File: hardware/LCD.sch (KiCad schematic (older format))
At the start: 0 parts

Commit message: Se finalizo esquematico del cricuito.
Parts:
- added DS1: LCD16X2, WC1602A, symbol LCD16X2
- added R7: 220, symbol R
- added RV1: 10k, symbol POT
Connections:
- new net: DS1.16 (LED-), R7.1
- new net: DS1.3 (VO), RV1.2
- new net +5V: DS1.15 (LED+), DS1.2 (VDD), RV1.1
- new net D1: DS1.11 (D4)
- new net D2: DS1.12 (D5)
- new net D3: DS1.13 (D6)
- new net D4: DS1.14 (D7)
- new net Ena: DS1.6 (E)
- new net GND: DS1.1 (VSS), DS1.10 (D3), DS1.5 (R/W), DS1.7 (D0), DS1.8 (D1), DS1.9 (D2), R7.2, RV1.3
- new net RS: DS1.4 (RS)
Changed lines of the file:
@@
 $Descr A4 11693 8268
 encoding utf-8
-Sheet 1 5
+Sheet 4 5
 Title ""
-Date ""
+Date "2016-07-04"
 Rev ""
-Comp ""
+Comp "Felipe Rey"
 Comment1 ""
 Comment2 ""
@@
 Comment4 ""
 $EndDescr
+$Comp
+L LCD16X2 DS1
+U 1 1 578E41A0
+P 5400 2050
+F 0 "DS1" H 4600 2450 50  0000 C CNN
+F 1 "LCD16X2" H 6100 2450 50  0000 C CNN
+F 2 "WC1602A" H 5400 2000 50  0000 C CIN
+F 3 "" H 5400 2050 50  0000 C CNN
+	1    5400 2050
+	1    0    0    -1
+$EndComp
+$Comp
+L GND #PWR016
+U 1 1 578E4217
+P 4650 3200
+F 0 "#PWR016" H 4650 2950 50  0001 C CNN
+F 1 "GND" H 4650 3050 50  0000 C CNN
+F 2 "" H 4650 3200 50  0000 C CNN
+F 3 "" H 4650 3200 50  0000 C CNN
+	1    4650 3200
+	1    0    0    -1
+$EndComp
+Wire Wire Line
+	4650 2550 4650 3200
+Wire Wire Line
+	5050 2550 5050 2850
+Wire Wire Line
+	4650 2850 5550 2850
+Connection ~ 4650 2850
+$Comp
+L +5V #PWR017
+U 1 1 578E4237
+P 4200 2150
+F 0 "#PWR017" H 4200 2000 50  0001 C CNN
+F 1 "+5V" H 4200 2290 50  0000 C CNN
+F 2 "" H 4200 2150 50  0000 C CNN
+F 3 "" H 4200 2150 50  0000 C CNN
+	1    4200 2150
+	1    0    0    -1
+$EndComp
+Wire Wire Line
+	4750 2550 4750 2650
+Wire Wire Line
+	4750 2650 4200 2650
+Wire Wire Line
+	4200 2650 4200 2150
+$Comp
+L POT RV1
+U 1 1 578E43FF
+P 3550 2750
+F 0 "RV1" H 3550 2650 50  0000 C CNN
+F 1 "10k" H 3550 2750 50  0000 C CNN
+F 2 "" H 3550 2750 50  0000 C CNN
+F 3 "" H 3550 2750 50  0000 C CNN
+	1    3550 2750
+	0    1    1    0
+$EndComp
+Wire Wire Line
+	4850 2550 4850 2750
+Wire Wire Line
+	4850 2750 3700 2750
+Wire Wire Line
+	3550 3000 3550 3100
+Wire Wire Line
+	3550 3100 4650 3100
+Connection ~ 4650 3100
+Wire Wire Line
+	3550 2500 3550 2250
+Wire Wire Line
+	3550 2250 4200 2250
+Connection ~ 4200 2250
+$Comp
+L +5V #PWR018
+U 1 1 578E496B
+P 6600 2250
+F 0 "#PWR018" H 6600 2100 50  0001 C CNN
+F 1 "+5V" H 6600 2390 50  0000 C CNN
+F 2 "" H 6600 2250 50  0000 C CNN
+F 3 "" H 6600 2250 50  0000 C CNN
+	1    6600 2250
+	1    0    0    -1
+$EndComp
+Wire Wire Line
+	6600 2250 6600 2700
+Wire Wire Line
+	6600 2700 6050 2700
+Wire Wire Line
+	6050 2700 6050 2550
+$Comp
+L R R7
+U 1 1 578E4997
+P 6150 3050
+F 0 "R7" V 6230 3050 50  0000 C CNN
+F 1 "220" V 6150 3050 50  0000 C CNN
+F 2 "" V 6080 3050 50  0000 C CNN
+F 3 "" H 6150 3050 50  0000 C CNN
+	1    6150 3050
+	1    0    0    -1
+$EndComp
+Wire Wire Line
+	6150 2550 6150 2900
+$Comp
+L GND #PWR019
+U 1 1 578E49E7
+P 6150 3400
+F 0 "#PWR019" H 6150 3150 50  0001 C CNN
+F 1 "GND" H 6150 3250 50  0000 C CNN
+F 2 "" H 6150 3400 50  0000 C CNN
+F 3 "" H 6150 3400 50  0000 C CNN
+	1    6150 3400
+	1    0    0    -1
+$EndComp
+Wire Wire Line
+	6150 3400 6150 3200
+Text HLabel 4950 3450 3    60   Input ~ 0
+RS
+Wire Wire Line
+	4950 2550 4950 3450
+Text HLabel 5150 3450 3    60   Input ~ 0
+Ena
+Wire Wire Line
+	5150 2550 5150 3450
+Text HLabel 5650 3500 3    60   Input ~ 0
+D1
+Text HLabel 5750 3500 3    60   Input ~ 0
+D2
+Text HLabel 5850 3500 3    60   Input ~ 0
+D3
+Text HLabel 5950 3500 3    60   Input ~ 0
+D4
+Wire Wire Line
+	5650 2550 5650 3500
+Wire Wire Line
+	5750 2550 5750 3500
+Wire Wire Line
+	5850 2550 5850 3500
+Wire Wire Line
+	5950 2550 5950 3500
+Wire Wire Line
+	5250 2850 5250 2550
+Connection ~ 5050 2850
+Wire Wire Line
+	5350 2850 5350 2550
+Connection ~ 5250 2850
+Wire Wire Line
+	5450 2850 5450 2550
+Connection ~ 5350 2850
+Wire Wire Line
+	5550 2850 5550 2550
+Connection ~ 5450 2850
 $EndSCHEMATC

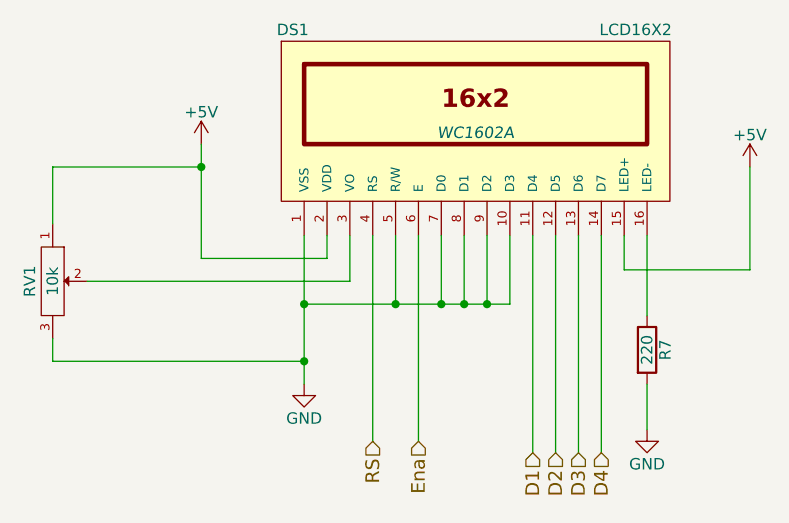
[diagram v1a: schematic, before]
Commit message: Se cargaron los footprint de los componentes.
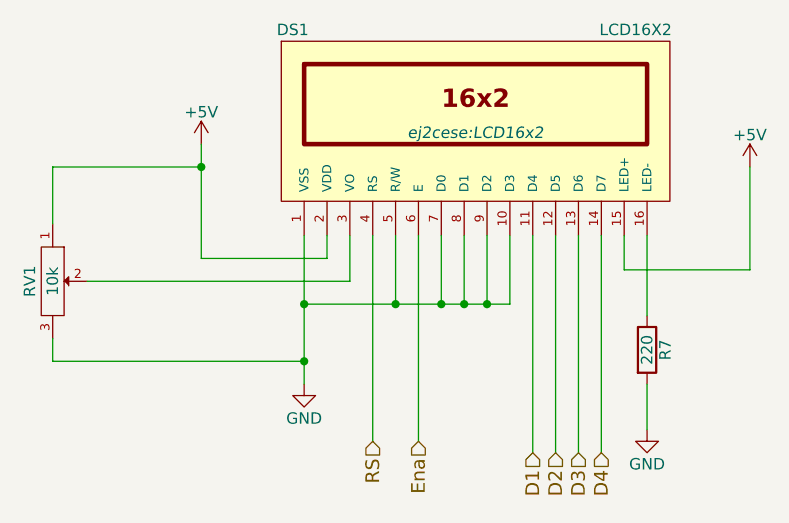
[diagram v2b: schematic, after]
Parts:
- DS1: footprint WC1602A -> ej2cese:LCD16x2
- R7: footprint (none) -> ej2cese:R_1206_HandSoldering
- RV1: footprint (none) -> SMD_Packages:POT_SMD
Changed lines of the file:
@@
 LIBS:valves
 LIBS:ej2cese
+LIBS:ADS1113IDGSR
 LIBS:poncho_celda-cache
 EELAYER 25 0
@@
 encoding utf-8
 Sheet 4 5
-Title ""
+Title "Diagrama de conexion a una LCD 16x2"
 Date "2016-07-04"
 Rev ""
@@
 F 0 "DS1" H 4600 2450 50  0000 C CNN
 F 1 "LCD16X2" H 6100 2450 50  0000 C CNN
-F 2 "WC1602A" H 5400 2000 50  0000 C CIN
+F 2 "ej2cese:LCD16x2" H 5400 2000 50  0000 C CIN
 F 3 "" H 5400 2050 50  0000 C CNN
 	1    5400 2050
@@
 F 0 "RV1" H 3550 2650 50  0000 C CNN
 F 1 "10k" H 3550 2750 50  0000 C CNN
-F 2 "" H 3550 2750 50  0000 C CNN
+F 2 "SMD_Packages:POT_SMD" H 3550 2750 50  0001 C CNN
 F 3 "" H 3550 2750 50  0000 C CNN
 	1    3550 2750
@@
 F 0 "R7" V 6230 3050 50  0000 C CNN
 F 1 "220" V 6150 3050 50  0000 C CNN
-F 2 "" V 6080 3050 50  0000 C CNN
+F 2 "ej2cese:R_1206_HandSoldering" V 6080 3050 50  0001 C CNN
 F 3 "" H 6150 3050 50  0000 C CNN
 	1    6150 3050
